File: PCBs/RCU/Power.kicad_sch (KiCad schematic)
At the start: 29 parts

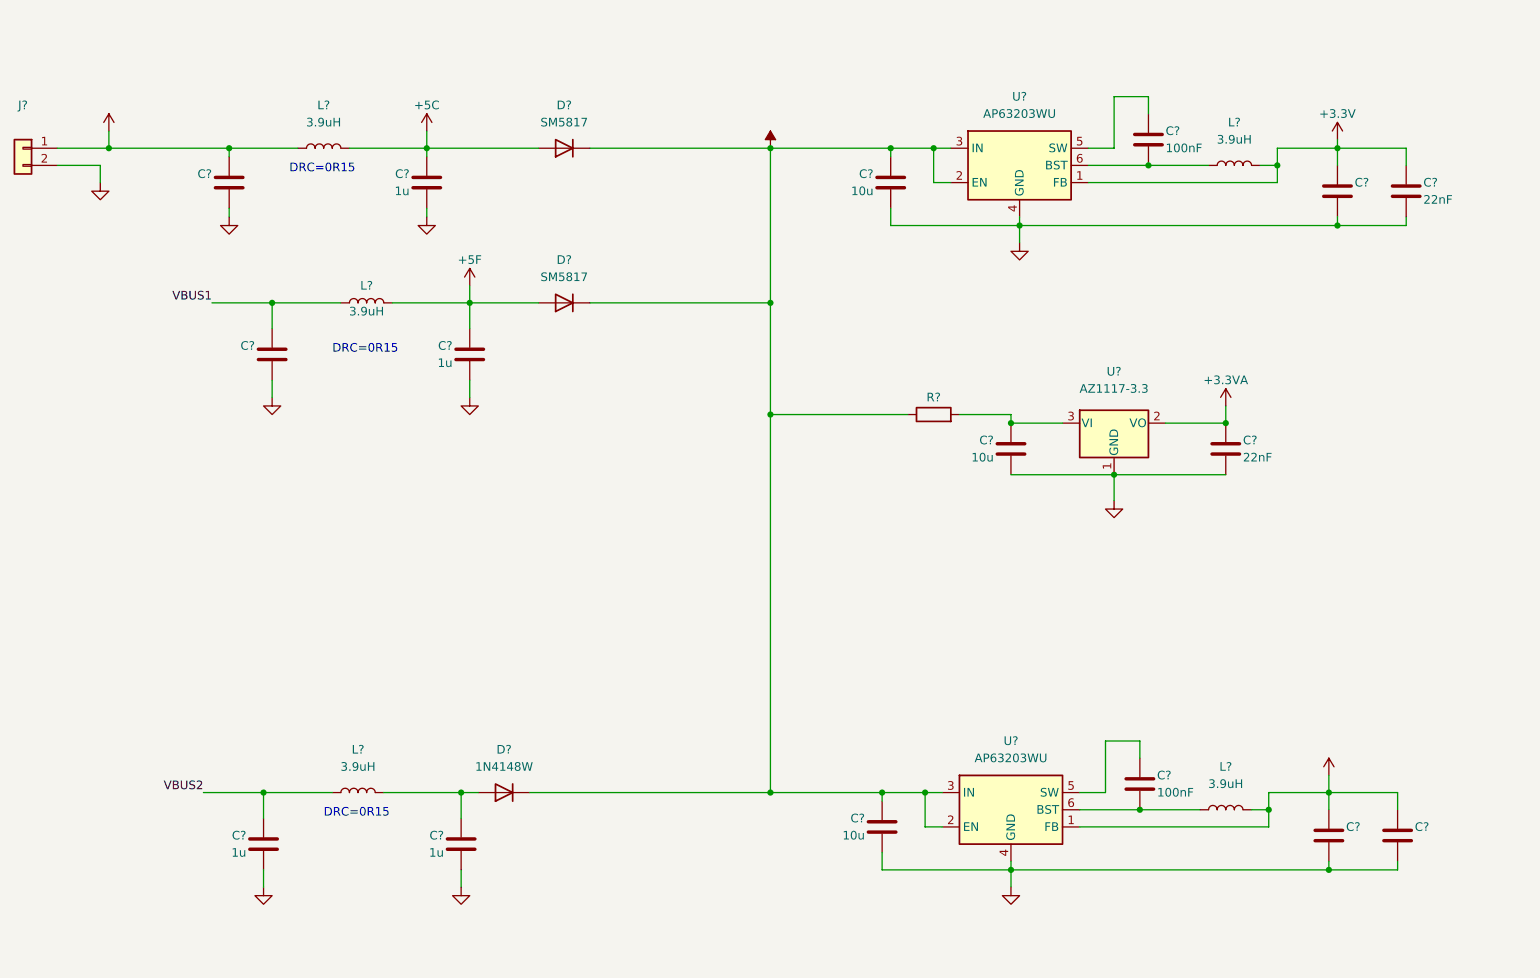
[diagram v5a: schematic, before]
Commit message: Numbered and ordered all of the modules
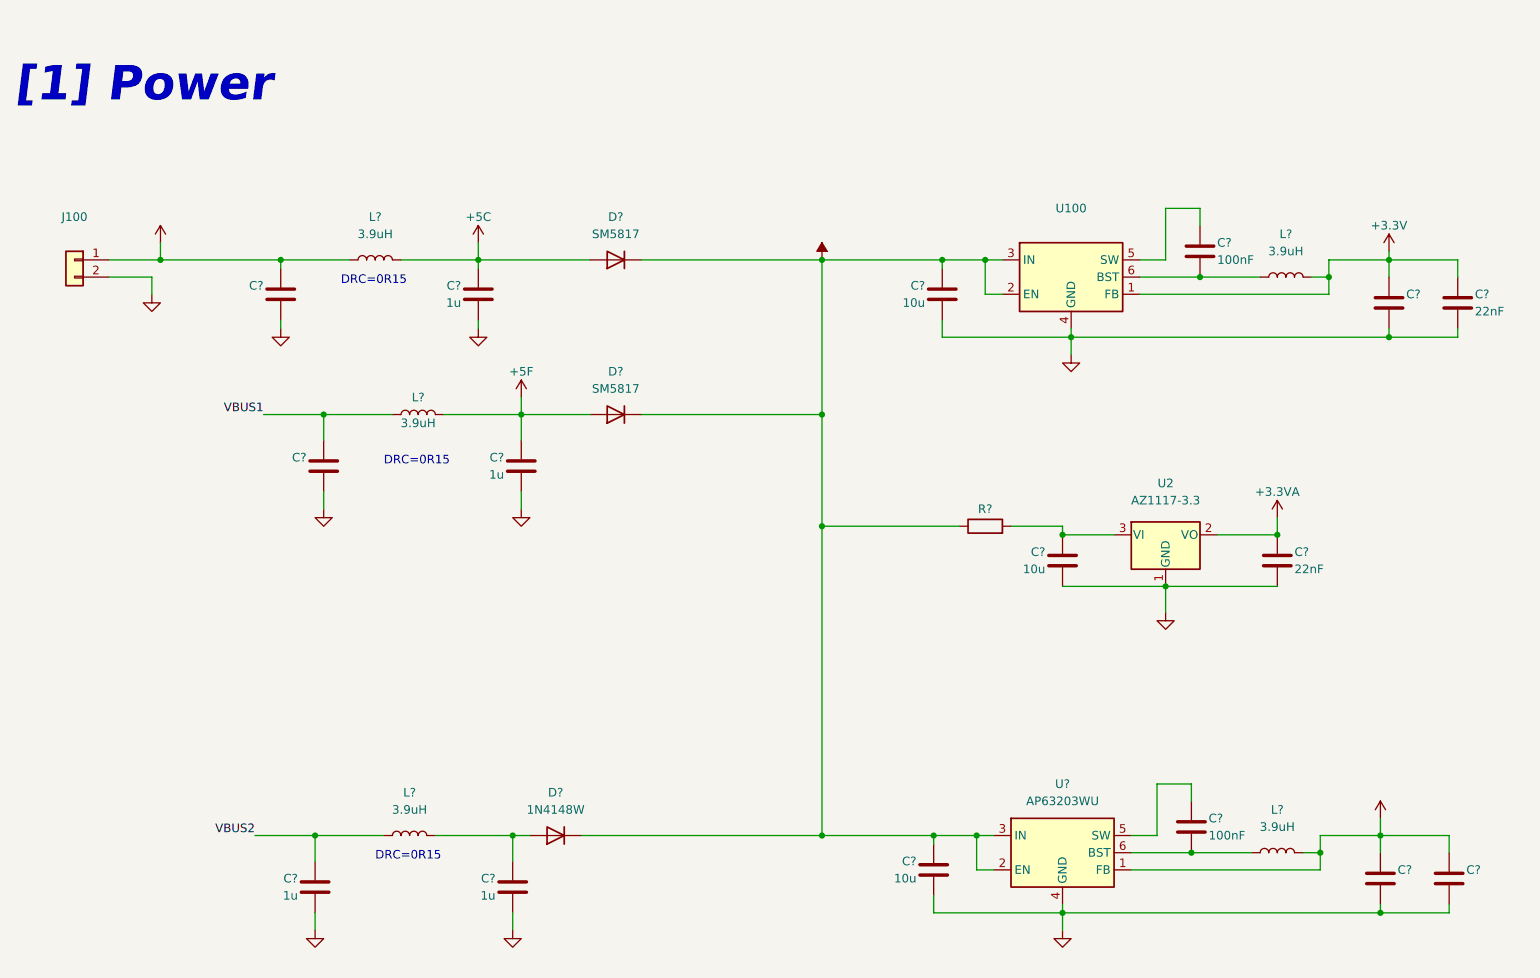
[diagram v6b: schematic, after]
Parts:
- U100: renamed from U?; value AP63203WU -> (none); footprint Package_TO_SOT_SMD:TSOT-23-6 -> (none)
- gave numbers to parts that had none: 2
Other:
- note added: "[1] Power"
- moved on the sheet: C?, D?, J100, L?, R?, U100, U2, U?

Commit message: Annotated all of the components in Power
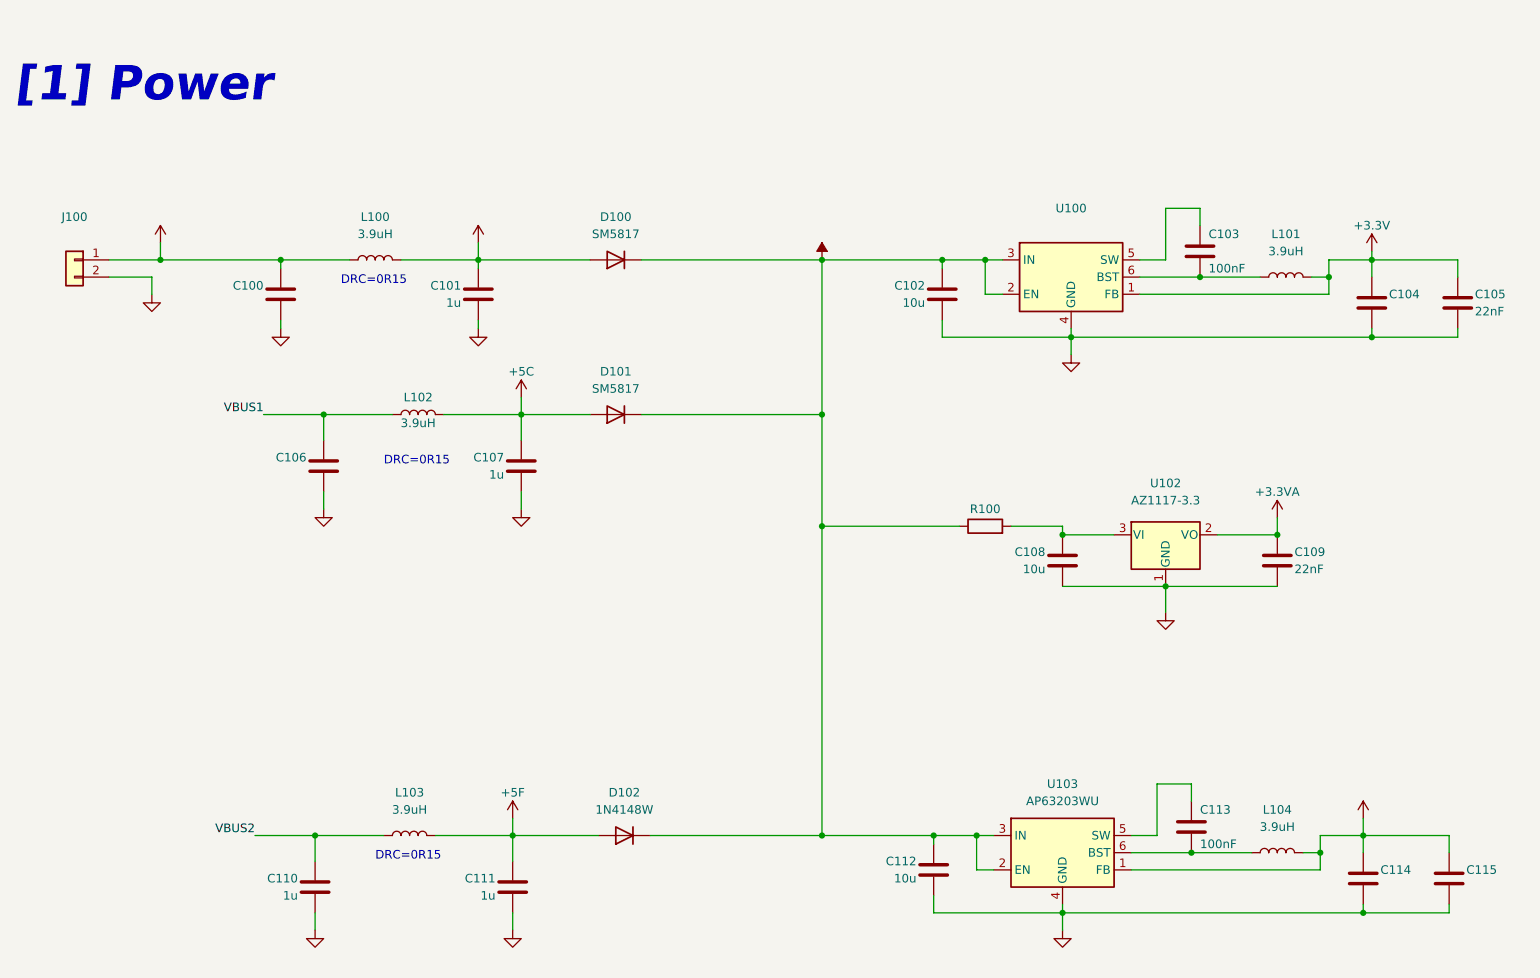
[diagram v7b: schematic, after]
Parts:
- gave numbers to parts that had none: 26
- renumbered U2 to U102
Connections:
- net +5C: now also C107.1, D101.2 (A), L102.2; no longer C101.1, D100.2 (A), L100.2
- net +5F: now also C111.1, D102.2 (A), L103.2; no longer C107.1, D101.2 (A), L102.2
- new net +9V: C101.1, D100.2 (A), L100.2
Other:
- moved on the sheet: C104, C114, D102

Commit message: Label power sub-circuits
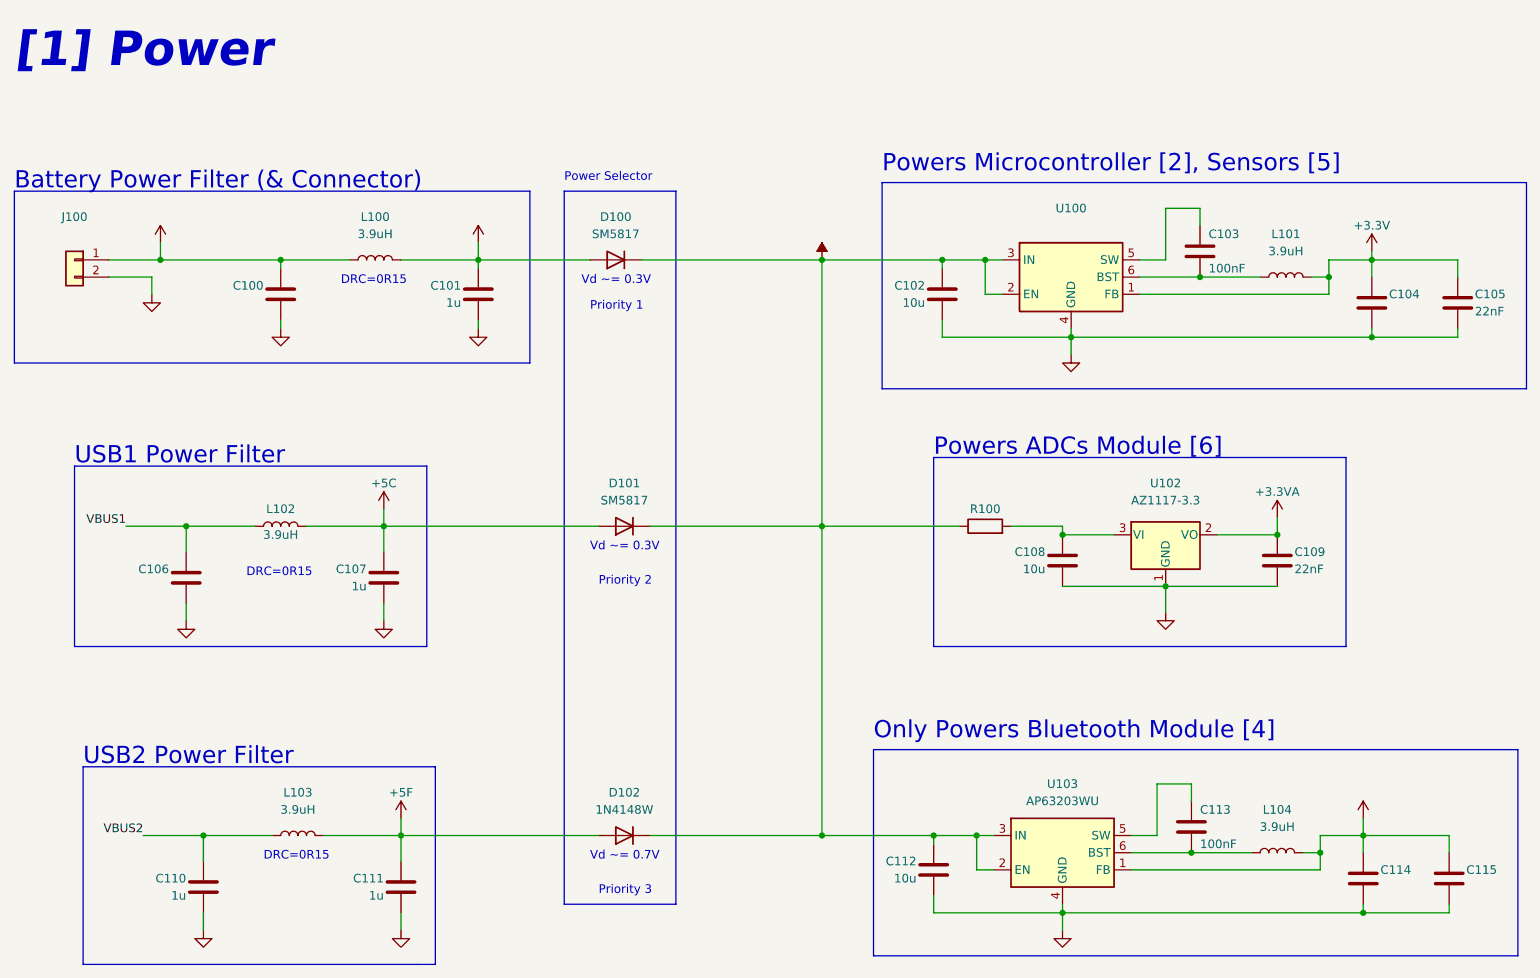
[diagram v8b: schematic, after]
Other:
- note added: "Battery Power Filter (& Connector)"
- note added: "Only Powers Bluetooth Module [4]"
- note added: "Power Selector"
- note added: "Powers ADCs Module [6]"
- note added: "Powers Microcontroller [2], Sensors [5]"
- note added: "Priority 1"
- note added: "Priority 2"
- note added: "Priority 3"
- note added: "USB1 Power Filter"
- note added: "USB2 Power Filter"
- note added: "Vd ~= 0.3V"
- note added: "Vd ~= 0.7V"
- moved on the sheet: C106, C107, C110, C111, D101, L102, L103
